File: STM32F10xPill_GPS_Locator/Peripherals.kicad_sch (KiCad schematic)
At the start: 26 parts, among them J1 Antenna, U2 QMC5883P, U3 AT2659, U4 ATGM336H-5N31

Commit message: Add all footprints and symbols, retouch schametic
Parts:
- J4: renamed from J1; value Antenna -> 734120110; LCSC Part (none) -> C434806
- JP3: renamed from JP5; footprint (none) -> Jumper:SolderJumper-2_P1.3mm_Open_Pad1.0x1.5mm
- JP4: renamed from JP2; footprint (none) -> Jumper:SolderJumper-2_P1.3mm_Open_Pad1.0x1.5mm
- JP5: renamed from JP1; footprint (none) -> Jumper:SolderJumper-3_P1.3mm_Open_Pad1.0x1.5mm_NumberLabels
- JP6: renamed from JP3; footprint (none) -> Jumper:SolderJumper-2_P1.3mm_Open_Pad1.0x1.5mm
- JP7: renamed from JP4; footprint (none) -> Jumper:SolderJumper-2_P1.3mm_Open_Pad1.0x1.5mm
- L2: renamed from L1; footprint (none) -> Inductor_SMD:L_0603_1608Metric; LCSC Part (none) -> C882493
- U6: renamed from U3; value AT2659 -> AT2659S; footprint Package_DFN_QFN:DFN-6_1.6x1.3mm_P0.4mm -> Package_TO_SOT_SMD:SOT-23-6; LCSC Part C92450 -> C883443
- renumbered C26 to C20, C12 to C21, C13 to C22, C14 to C23, C15 to C24, C16 to C25, C17 to C26, D2 to D5, NT3 to NT5, R18 to R22, R6 to R23, TP9 to TP17, TP7 to TP18, TP8 to TP19, TP6 to TP20, U7 to U4, U2 to U5, U4 to U7
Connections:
- net +BATT is gone; now on net +3.3V: JP6.1 (A)
- net +3.3V: no longer JP3.1 (A), JP4.1 (A), JP7.1 (A)
- new net +3.3V_SW: JP3.1 (A), JP4.1 (A), JP7.1 (A)
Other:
- note added: "LQG18HN6N8J00D"

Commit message: Begin PCB layout
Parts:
- added H1, H2, H3, H4: MountingHole, MountingHole:MountingHole_2.2mm_M2, symbol Mechanical:MountingHole
- U4: footprint Connector_JST:JST_XH_B8B-XH-A_1x08_P2.50mm_Vertical -> Connector_PinSocket_2.54mm:PinSocket_1x08_P2.54mm_Vertical

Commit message: Initial placement completed
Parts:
- renumbered C20 to C21, C21 to C22, C22 to C23, C23 to C24, C24 to C25, C25 to C26, C26 to C27, R22 to R23, R23 to R24, TP17 to TP13, TP18 to TP14, TP19 to TP15, TP20 to TP16
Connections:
- net +3.3V: no longer U6.5 (nSHDN)
- net LNA_VCC: now also U6.5 (nSHDN)

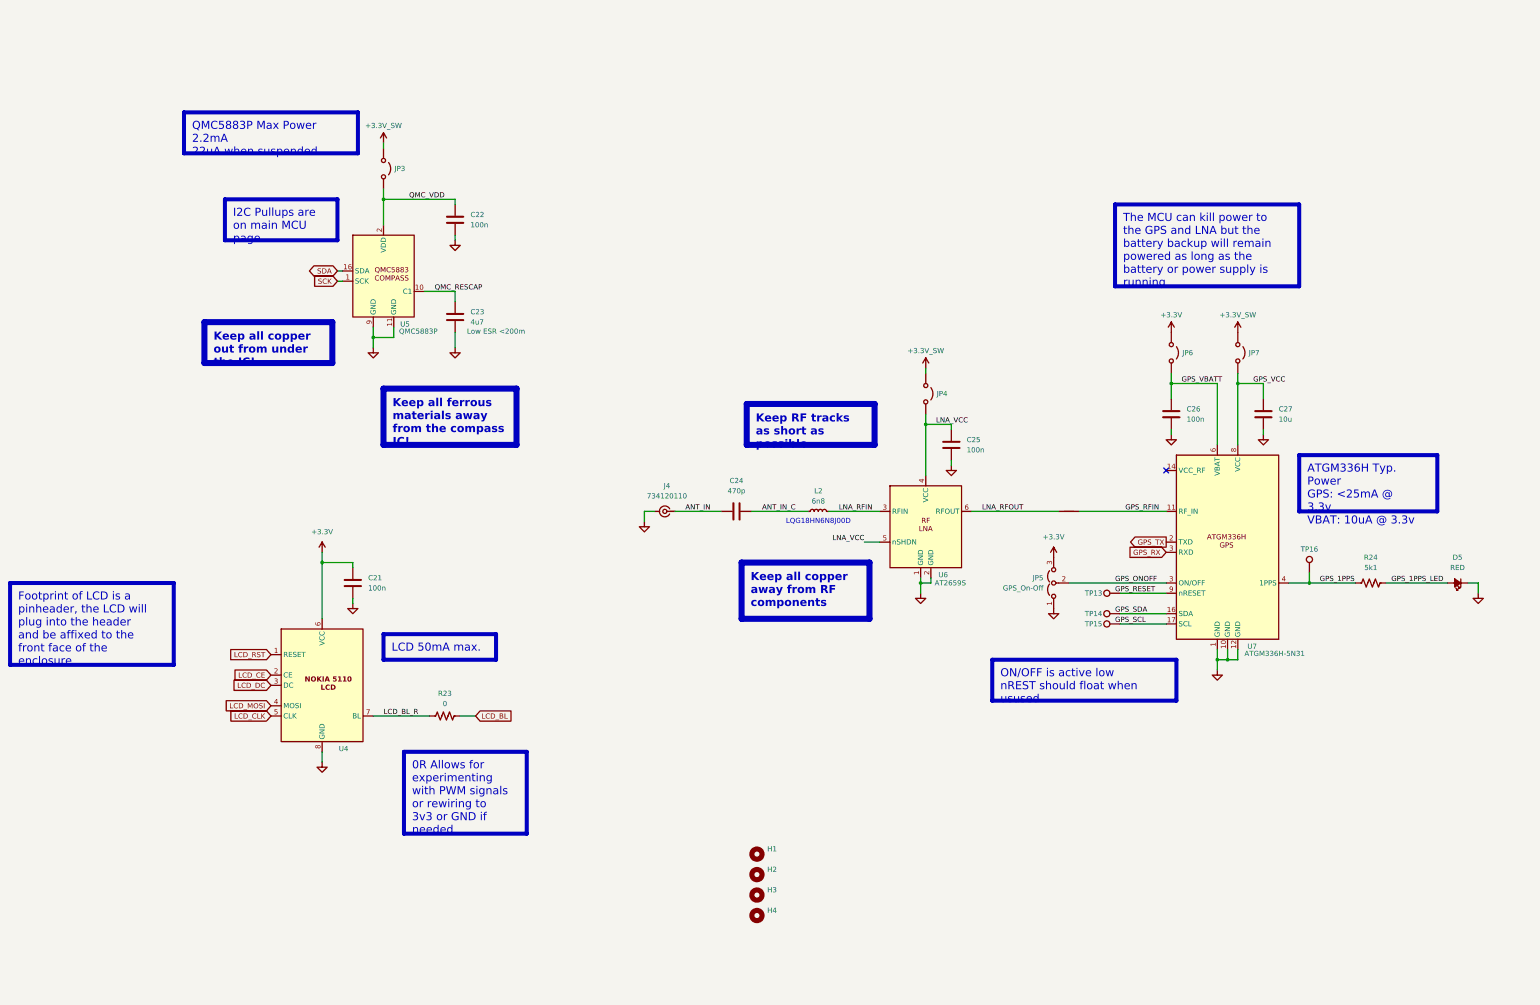
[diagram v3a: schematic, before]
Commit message: Add USB Port
Added schematic for controlling SEL and PROG2 on the PPM, as well as USB filtering and ESD protection and stuff. The board layout was not changed yet
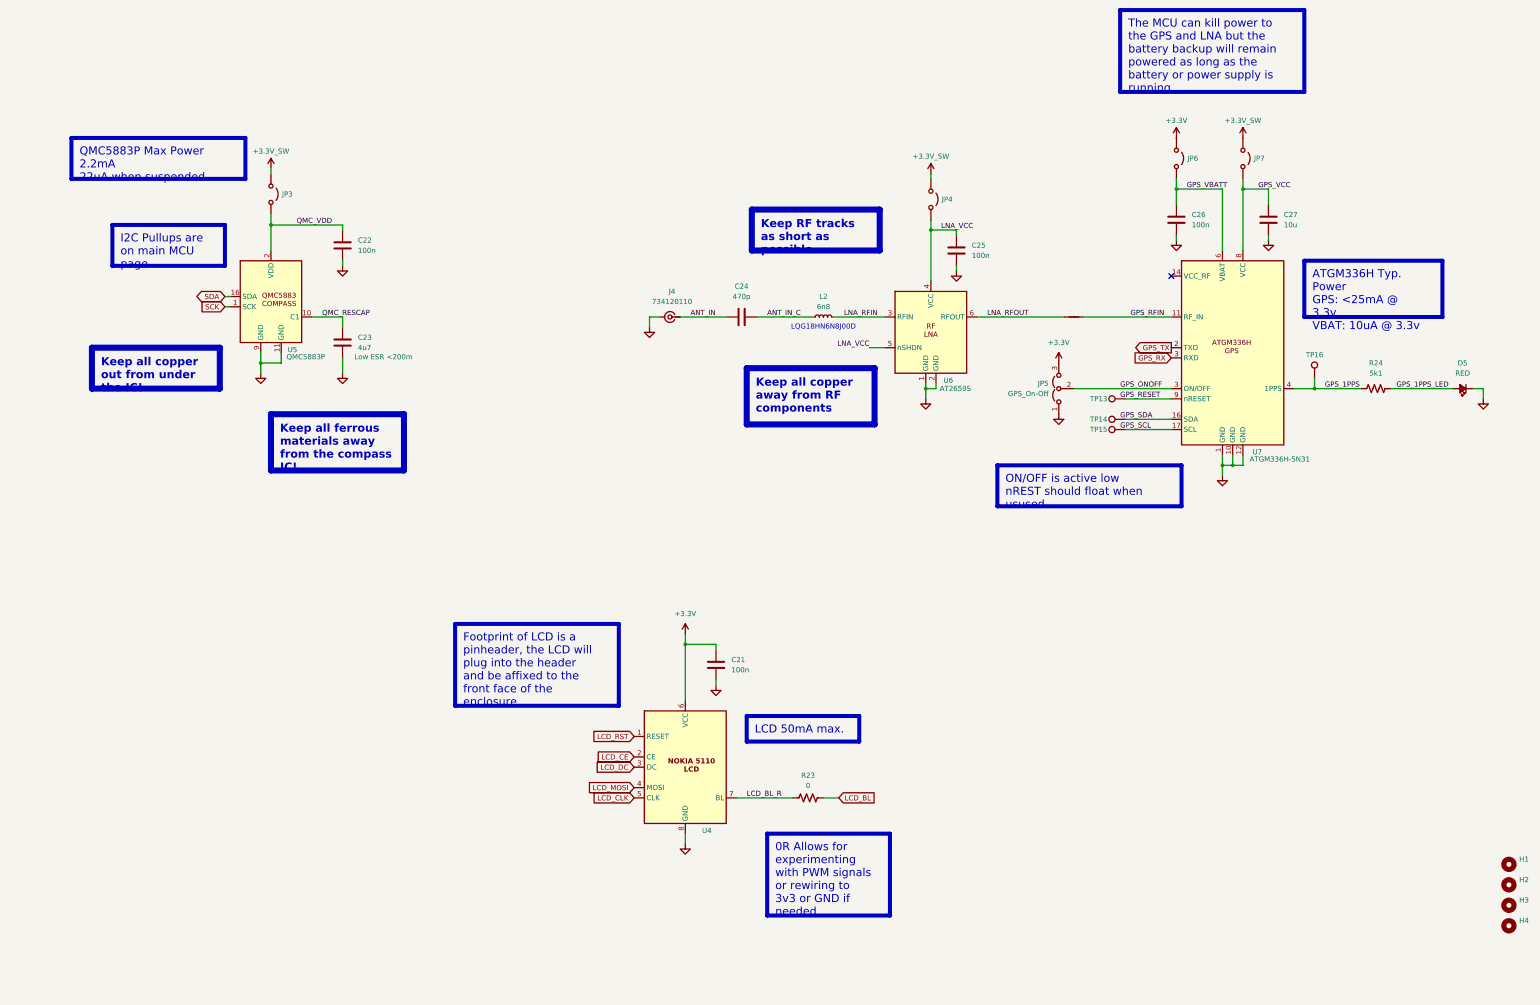
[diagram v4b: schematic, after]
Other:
- moved on the sheet: C21, C22, C23, C24, C25, C26, C27, D5, H1, H2, H3, H4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

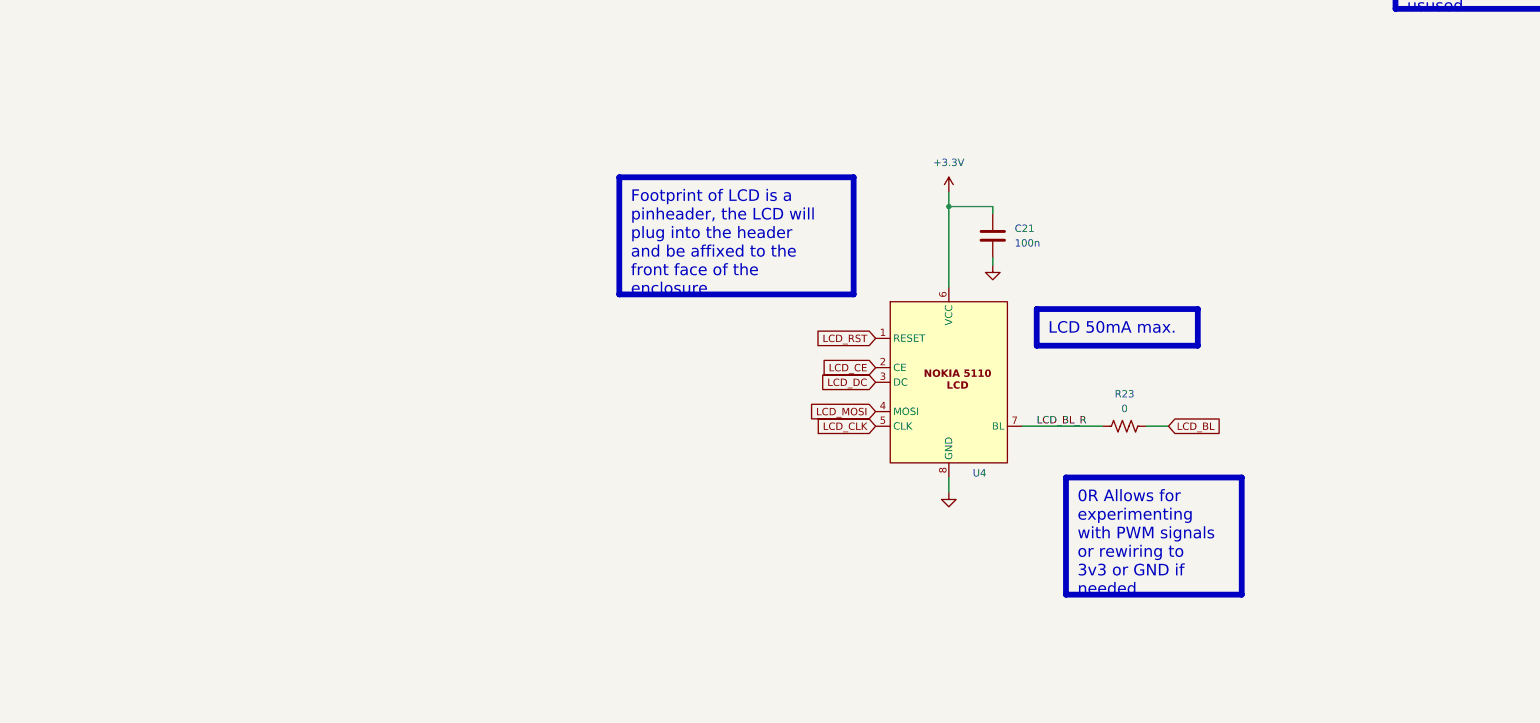
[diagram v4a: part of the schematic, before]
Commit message: Added SD card and updated PCB layout
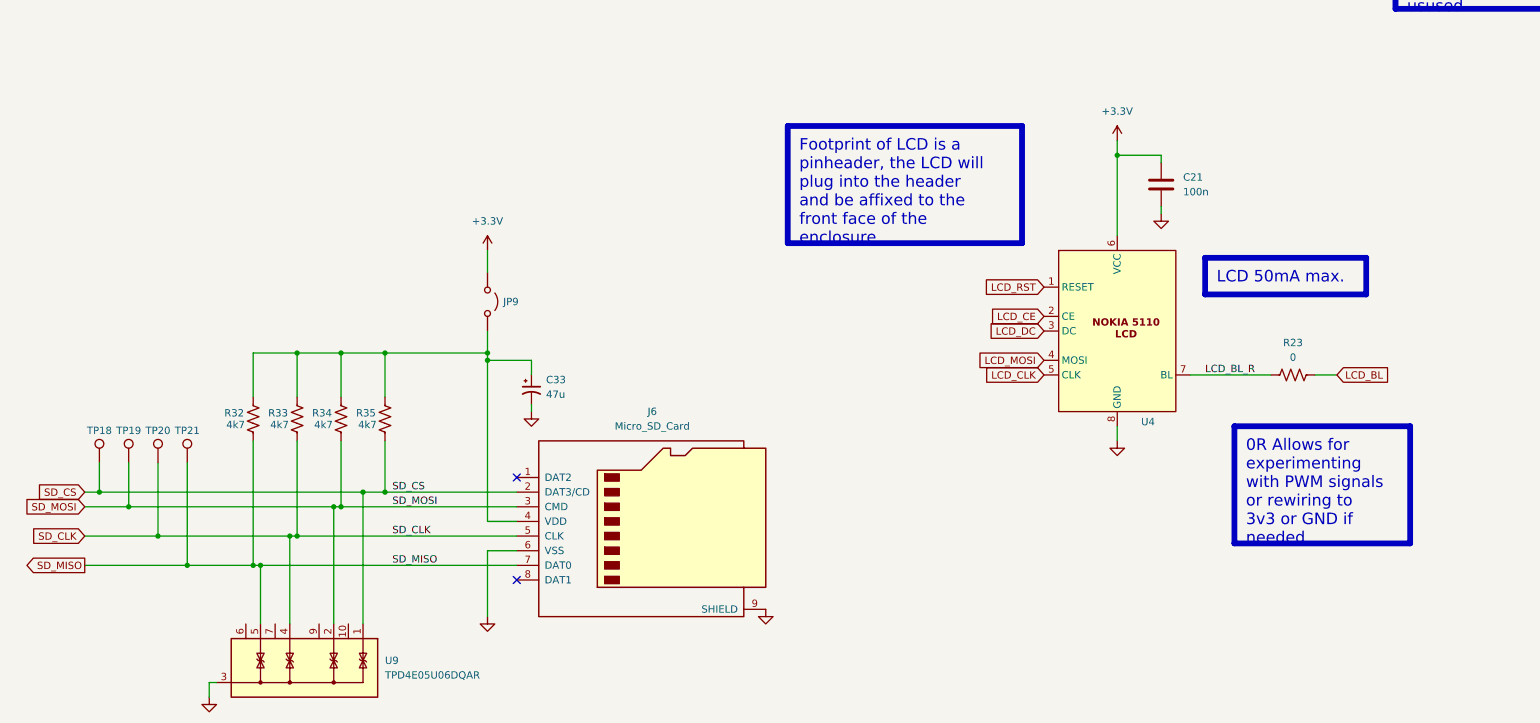
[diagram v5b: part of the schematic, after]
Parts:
- added C33: 47u, Capacitor_SMD:CP_Elec_4x5.4, symbol Device:C_Polarized_Small_US
- added J6: Micro_SD_Card, Connector_Card:microSD_HC_Hirose_DM3AT-SF-PEJM5, symbol Connector:Micro_SD_Card
- added JP9: Jumper_2_Open, Jumper:SolderJumper-2_P1.3mm_Open_Pad1.0x1.5mm, symbol Jumper:Jumper_2_Open
- added R32, R33, R34, R35: 4k7, Resistor_SMD:R_0402_1005Metric_Pad0.72x0.64mm_HandSolder, symbol Device:R_US
- added TP18: SD_CS, TestPoint:TestPoint_Pad_D1.5mm, symbol Connector:TestPoint
- added TP19: SD_MOSI, TestPoint:TestPoint_Pad_D1.5mm, symbol Connector:TestPoint
- added TP20: SD_CLK, TestPoint:TestPoint_Pad_D1.5mm, symbol Connector:TestPoint
- added TP21: SD_MISO, TestPoint:TestPoint_Pad_D1.5mm, symbol Connector:TestPoint
- added U9: TPD4E05U06DQAR, Package_DFN_QFN:Diodes_UDFN-10_1.0x2.5mm_P0.5mm, symbol Power_Protection:TPD4E02B04DQA
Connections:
- net +3.3V: now also JP9.1 (A)
- net GND: now also C33.2, J6.6 (VSS), J6.9 (SHIELD), U9.3 (G), U9.8 (G)
- new net: C33.1, J6.4 (VDD), JP9.2 (B), R32.2, R33.2, R34.2, R35.2
- new net SD_CLK: J6.5 (CLK), R33.1, TP20.1, U9.4 (IO3)
- new net SD_CS: J6.2 (DAT3/CD), R35.1, TP18.1, U9.1 (IO1)
- new net SD_MISO: J6.7 (DAT0), R32.1, TP21.1, U9.5 (IO4)
- new net SD_MOSI: J6.3 (CMD), R34.1, TP19.1, U9.2 (IO2)
- no-connect marks 1 -> 3
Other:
- moved on the sheet: C21, R23, U4
